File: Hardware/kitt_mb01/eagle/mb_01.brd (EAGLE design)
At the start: 58.4 x 53.3 mm, 126 parts, among them IC2.0 BQ24266RGET, IC3.01 LSM9DS1, U1.01 RT8293A, U1.02 MIC5205-3.3YM5TR, U6.01 TPS61032RSARPSDO-G16, U7.01 SI1922EDH, U7.03 SI1922EDH, U7.2 SI1922EDH, X2.01 S2B-PH-K-S(LF)(SN), X7.02 ARDUINO_UNO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

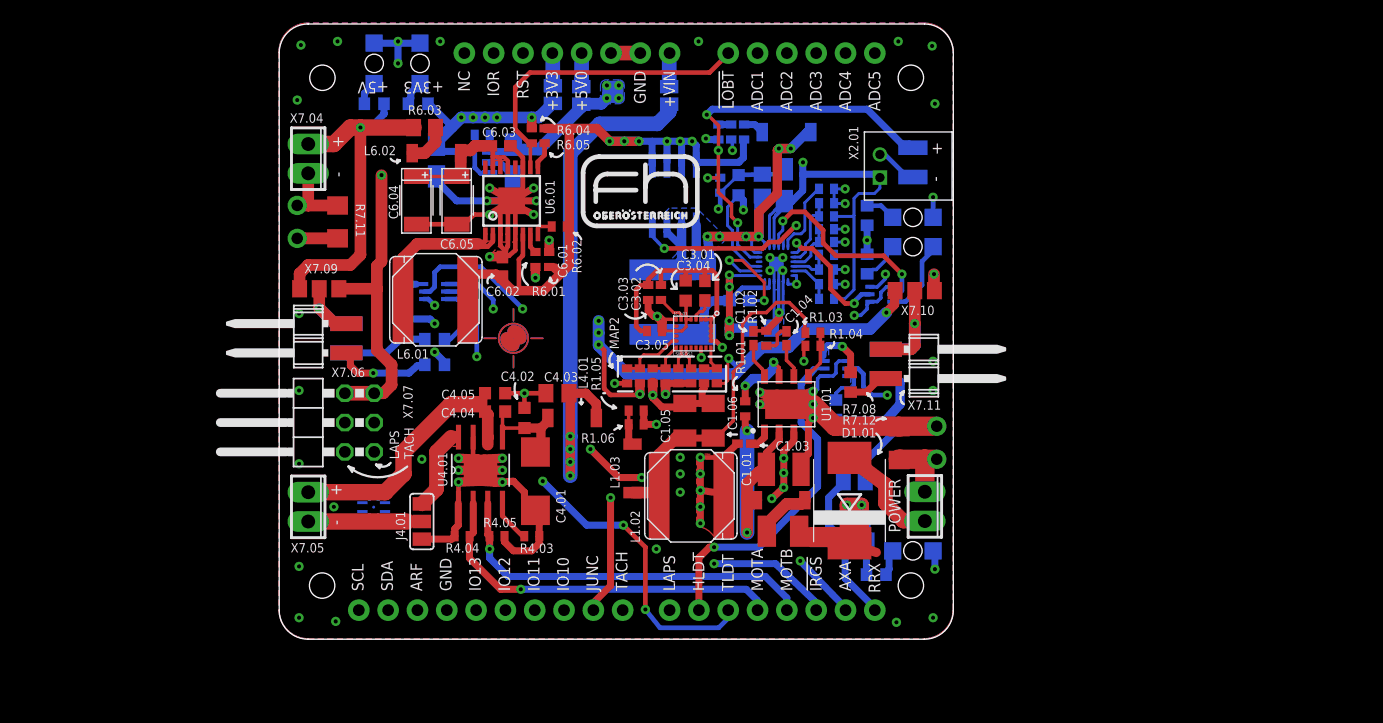
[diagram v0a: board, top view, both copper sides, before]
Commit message: -> added missing i2c routes -> rearranged inductor for battery charger to be in lesser proximity to the gyro
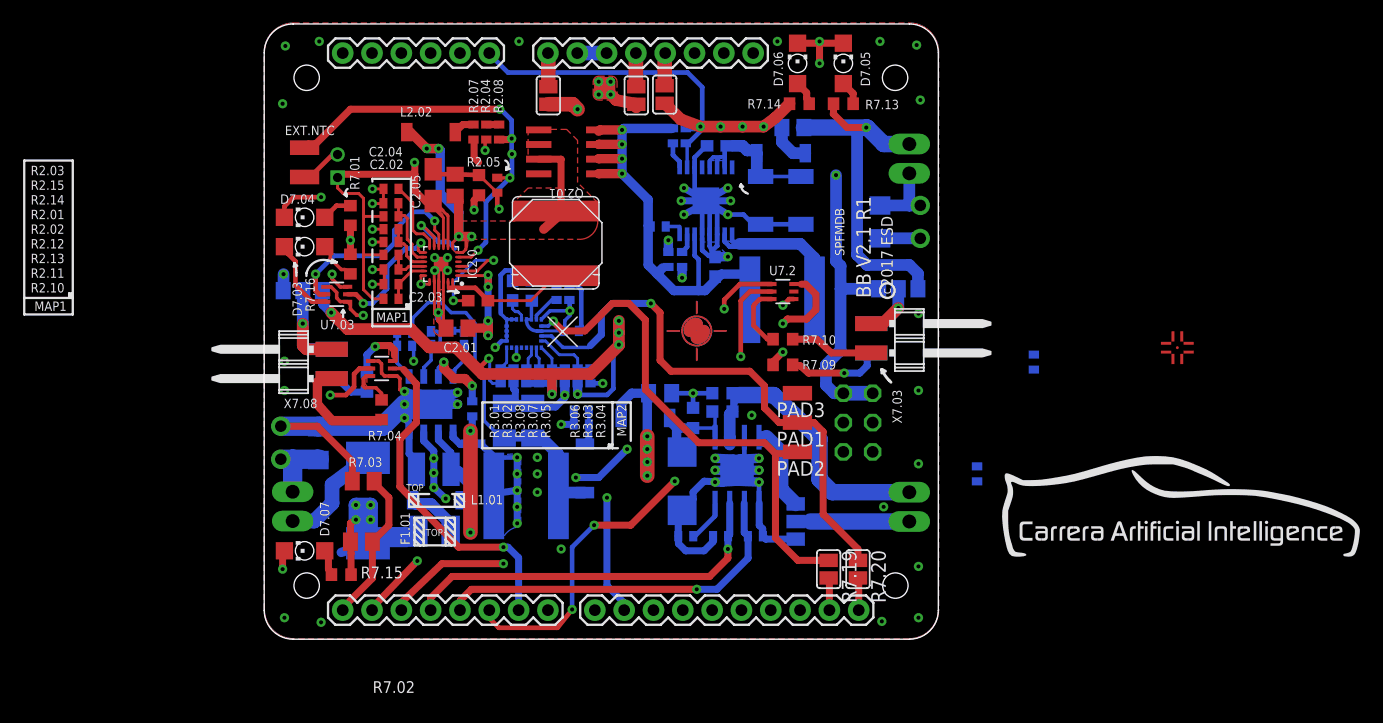
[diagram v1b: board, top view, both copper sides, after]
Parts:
- removed C1.07, C1.08: 1uF, rcl:A/3216-18R
- removed R1.07: [0R], rcl:R0402
- removed U1.02: MIC5205-3.3YM5TR, kitt.ic:SOT95P280X130-5N
- added PAD1, PAD2, PAD3: (no value), wirepad:SMD1,27-2,54
- added R7.17, R7.18: 10kR, rcl:R0402
- added R7.19, R7.20: [0R], jumper:SJ
- moved U$8 71.0 mm to (124.5, 45.9), flipped to the top
- moved DCL2 57.0 mm to (124.6, 30.3), flipped to the top
- moved X7.01 54.8 mm to (47.9, 32.1), flipped to the bottom
- moved X7.07 53.3 mm to (101.9, 39.4), flipped to the bottom
- moved X7.10 53.0 mm to (48.7, 50.8), flipped to the bottom
- moved D7.03 52.7 mm to (48.9, 54.6), flipped to the top
- moved D7.04 52.7 mm to (48.9, 57.1), flipped to the top
- moved D7.07 52.7 mm to (48.9, 28.3), flipped to the top
- moved NTC+ 52.7 mm to (48.9, 63.2), flipped to the top
- moved NTC- 52.7 mm to (48.9, 60.6), flipped to the top
- moved X7.04 52.1 mm to (101.3, 62.2), flipped to the bottom
- moved X7.05 52.1 mm to (101.3, 32.1), flipped to the bottom
- moved R7.12 50.3 mm to (50.1, 37.5), flipped to the bottom
- moved X7.09 50.2 mm to (100.3, 51.0), flipped to the bottom
- moved X7.08 49.5 mm to (50.5, 44.5), flipped to the top
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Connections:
- removed net ARDUINO.SCL: IC3.01.2
- removed net ARDUINO.SDA: IC3.01.4
- removed net SCL: X7.02.SCL
- removed net SDA: X7.02.SDA
- new net GYRO.SCL: IC3.01.2, PAD2.1, R7.17.1, R7.19.1
- new net GYRO.SDA: IC3.01.4, PAD1.1, R7.18.1, R7.20.1
- new net N$53: R7.20.2, X7.02.SCL
- net +3V3: now also R7.17.2, R7.18.2; no longer C1.08.+, U1.02.5
- net +5V: no longer C1.07.+, R1.07.2, U1.02.1
- net GND: now also PAD3.1; no longer C1.07.-, C1.08.-, U1.02.2
- net N$49: now also R7.19.2, X7.02.SDA; no longer R1.07.1, U1.02.3
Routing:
- net GYRO.SDA: track 0.00 -> 48.0 mm, vias 0 -> 1
- net GYRO.SCL: track 0.00 -> 46.8 mm, vias 0 -> 1
- net +12V: track 112.2 -> 153.8 mm, vias 8 -> 9
- net +5V: track 163.5 -> 144.1 mm
- net +4.1V: track 114.7 -> 97.0 mm, vias 7 -> 5
- net N$18: track 43.6 -> 30.3 mm, vias 6 -> 4
- net GND: track 257.9 -> 245.4 mm
- net N$14: track 17.1 -> 6.10 mm, vias 2 -> 1
- net CAR.AUXILLARY: track 53.6 -> 45.2 mm, vias 4 -> 3
- net V+: track 16.2 -> 8.90 mm
- net +3V3: track 159.2 -> 154.6 mm, vias 15 -> 14
- net N$53: track 0.00 -> 2.82 mm
- net N$33: track 25.0 -> 26.9 mm
- net N$49: track 4.34 -> 2.82 mm
- net N$15: track 37.3 -> 36.3 mm
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- added copper zone on layer 1, net +4.1V
- added copper zone on layer 1, net +5V
- added copper zone on layer 1, net CAR.FLIGHT
- added copper zone on layer 1, net N$18
- added copper zone on layer 1, net N$2
- added copper zone on layer 16, net N$34
- added copper zone on layer 16, net N$39
- added copper zone on layer 16, net N$43
- added copper zone on layer 1, net N$7
- added copper zone on layer 16, net N$88
- removed copper zone on layer 16, net +4.1V
- removed copper zone on layer 16, net +5V
- removed copper zone on layer 16, net CAR.FLIGHT
- removed copper zone on layer 16, net N$18
- removed copper zone on layer 16, net N$2
- removed copper zone on layer 1, net N$34
- removed copper zone on layer 1, net N$39
- removed copper zone on layer 1, net N$43
- removed copper zone on layer 16, net N$7
- removed copper zone on layer 1, net N$88
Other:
- board text added: "AUXILLARY PORTS ARE NOW ON DB02 AAAAAAAAA"
- board text added: "I BETTER PLACE AN AXIS GUIDE RIGHT HERE DAMNIT"
- board text added: "RAIL TEST POINTS!!!!"

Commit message: redid some routes, they seem more optimized
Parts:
- moved R7.17 25.1 mm to (94.3, 26.8)
- moved R7.18 13.1 mm to (96.8, 26.8), turned to 270 degrees
- moved L2.02 0.16 mm to (59.9, 64.7)
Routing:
- net +3V3: track 154.6 -> 173.6 mm, vias 14 -> 15
- net N$14: track 6.10 -> 18.3 mm, vias 1 -> 2
- net CAR.AUXILLARY: track 45.2 -> 53.0 mm, vias 3 -> 4
- net +4.1V: track 97.0 -> 91.5 mm
- net N$18: track 30.3 -> 32.8 mm
- net N$15: track 36.3 -> 38.2 mm
- net GYRO.SCL: track 46.8 -> 45.3 mm, vias 1 -> 2
- net GYRO.SDA: track 48.0 -> 49.2 mm, vias 1 -> 2
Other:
- board text added: "FIX UNINTENTIONAL SLOT ANTENNAE"

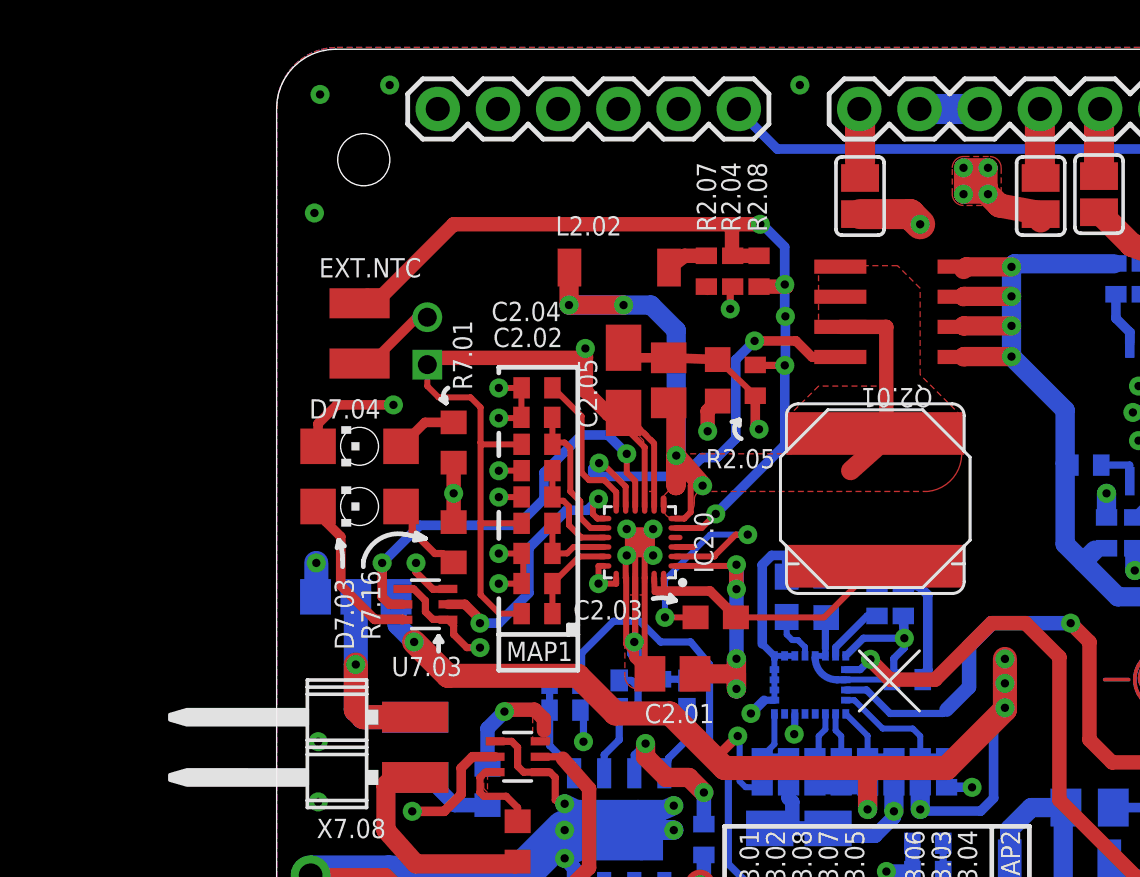
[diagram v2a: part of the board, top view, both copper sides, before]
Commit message: even more optimizations happened in subgroup 2XX -> less vias -> caps closer to IC -> added "hacking" resistor R213 to enable bodge-jobbing !CE
todo:
-> remove dots between identifiers to save precious silk screen real estate
-> run the DRC, plus ERC
-> scale down and re-place logo
-> more testpoints, it's low-effort for a potential high-payout when murphy strikes again
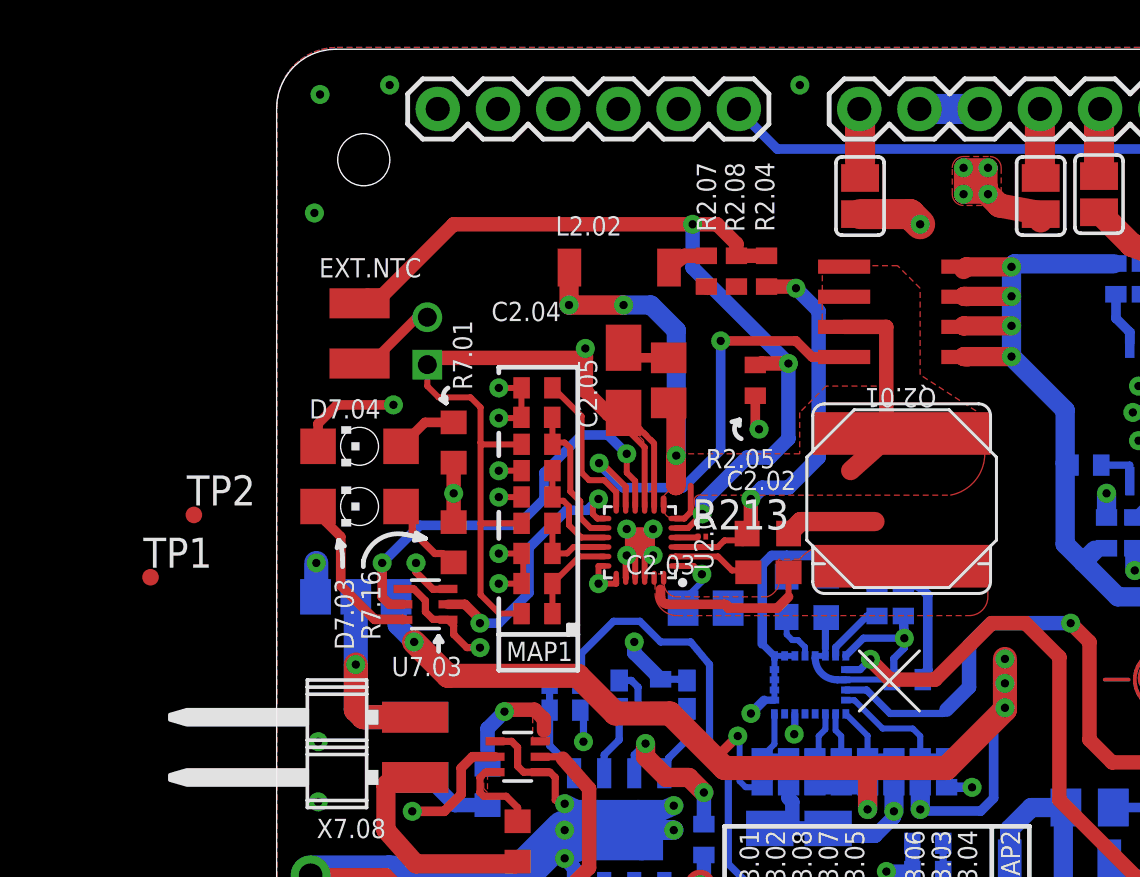
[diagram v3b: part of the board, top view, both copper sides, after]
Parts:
- added R213: [10k], rcl:R01005
- added TP1, TP2: TPTP07R, testpad:TP07R
- moved C2.02 6.80 mm to (66.1, 53.5), turned to 0 degrees
- moved C2.01 3.11 mm to (63.5, 50.3), flipped to the bottom
- moved C2.03 2.93 mm to (66.1, 51.8)
- moved R2.04 1.43 mm to (66.1, 64.5)
- moved L2.01 1.11 mm to (71.8, 55.2)
- moved R2.08 0.95 mm to (64.8, 64.5)
- moved Q2.01 0.16 mm to (71.9, 62.8)
- renumbered IC2.0 to U2.0
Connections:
- net N$12 renamed U2.0/SW
- net N$13 renamed U2.0/BOOT
- net N$14 renamed U2.0/BGATE
- net N$15 renamed U2.0/TS
- net N$18 renamed U2.0/SYS
- net N$8 renamed U2.0/PMID
- net V+ renamed U2.0/DRV
- new net N$8: R213.1, U2.0.4
- net GND: now also R213.2
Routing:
- net GND: track 245.4 -> 224.9 mm, vias 69 -> 68
- net U2.0/PMID: track 12.5 -> 3.18 mm, vias 4 -> 1
- net U2.0/DRV: track 8.90 -> 17.7 mm
- net U2.0/BOOT: track 10.6 -> 3.36 mm, vias 2 -> 0
- net U2.0/SW: track 12.2 -> 7.38 mm
- net U2.0/SYS: track 32.8 -> 31.3 mm, vias 4 -> 3
- net N$8: track 0.00 -> 0.97 mm
- net +4.1V: track 91.5 -> 92.1 mm
- net U2.0/BGATE: track 18.3 -> 19.0 mm
- net U2.0/TS: vias 4 -> 3
- added copper zone on layer 1, net U2.0/SW

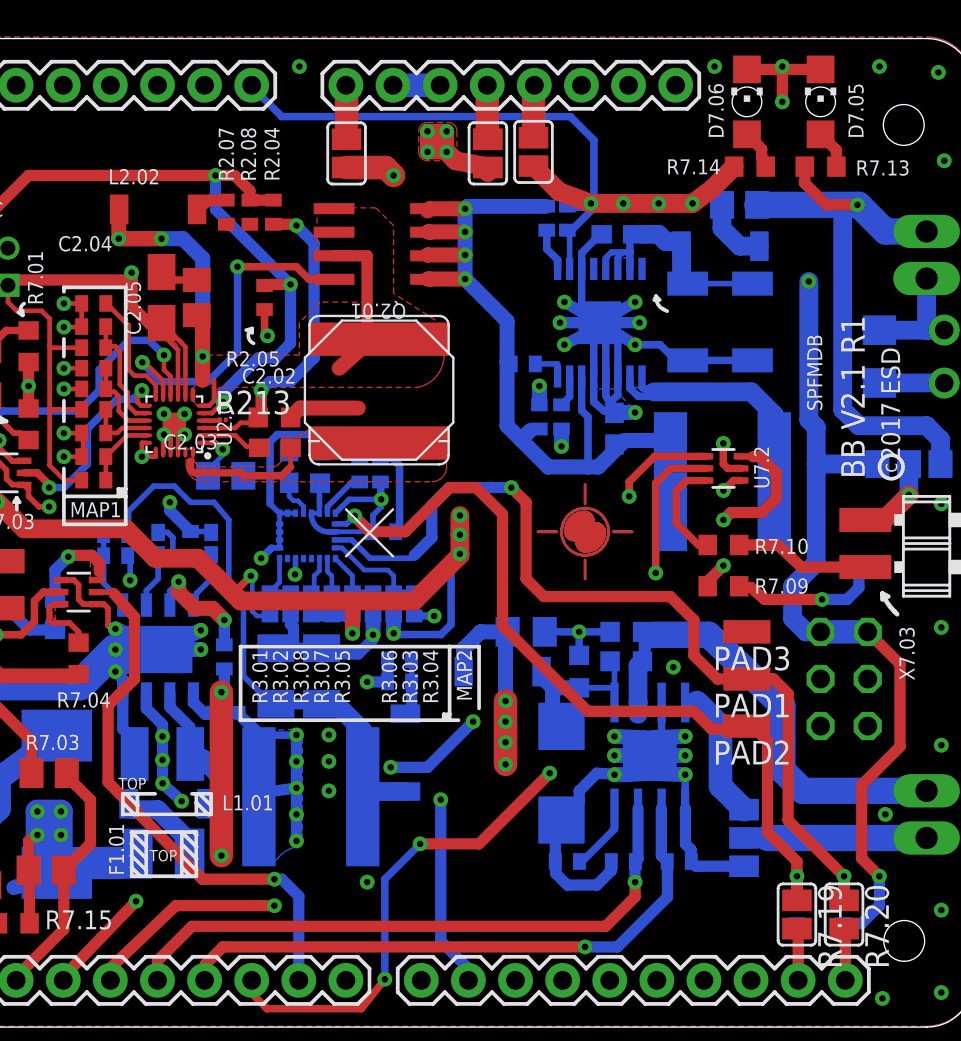
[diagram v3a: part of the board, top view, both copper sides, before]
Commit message: minor adjustments of power plane in northwest corner
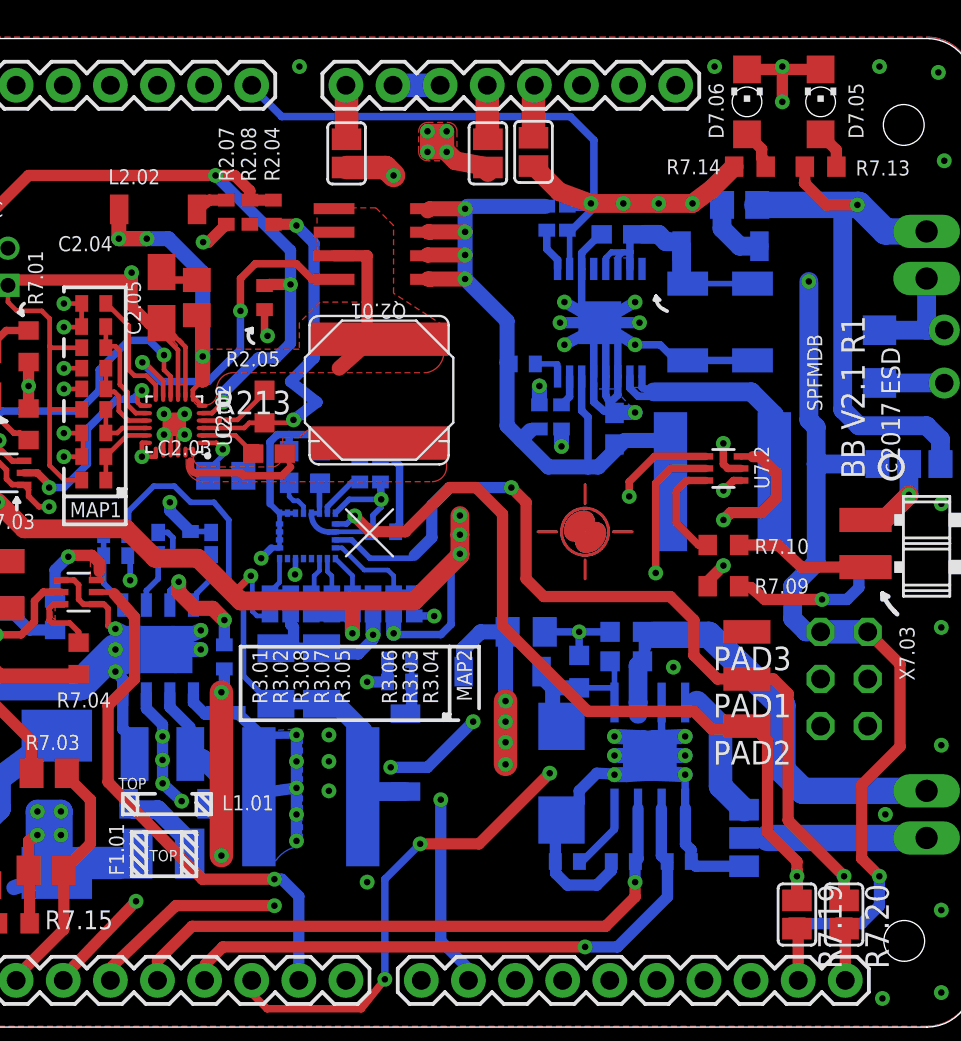
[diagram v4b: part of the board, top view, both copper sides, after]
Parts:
- moved C2.02 0.79 mm to (65.6, 54.1), turned to 90 degrees
- moved C2.03 0.45 mm to (65.8, 51.5)
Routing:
- net +3V3: track 173.6 -> 176.2 mm
- net U2.0/DRV: track 17.7 -> 19.4 mm
- net +4.1V: track 92.1 -> 93.8 mm, vias 5 -> 6
- net U2.0/SYS: track 31.3 -> 29.7 mm
